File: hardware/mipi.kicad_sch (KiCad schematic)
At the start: 52 parts, among them U4 CCGM1A1, Y1 FNETHE025

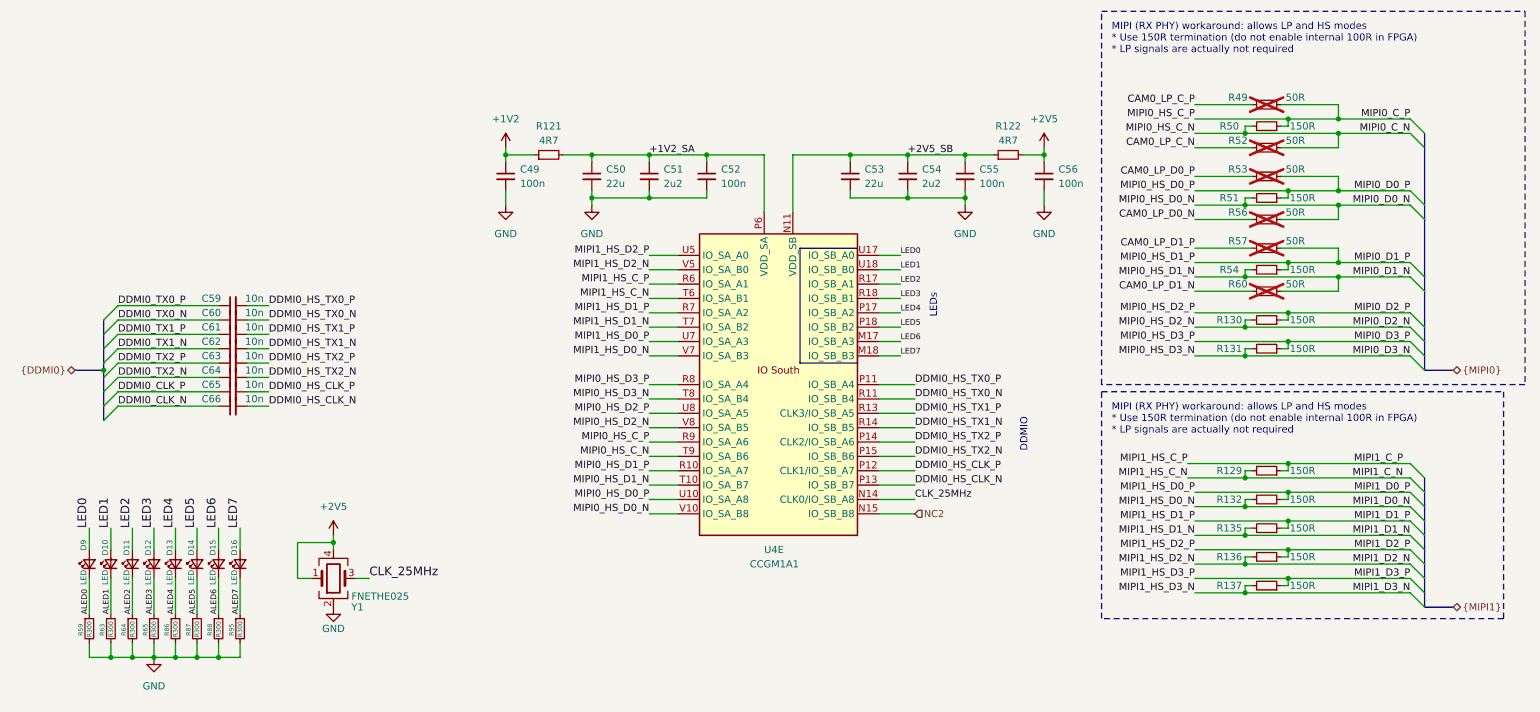
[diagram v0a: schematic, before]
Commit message: Clearing ERC errors/warnings
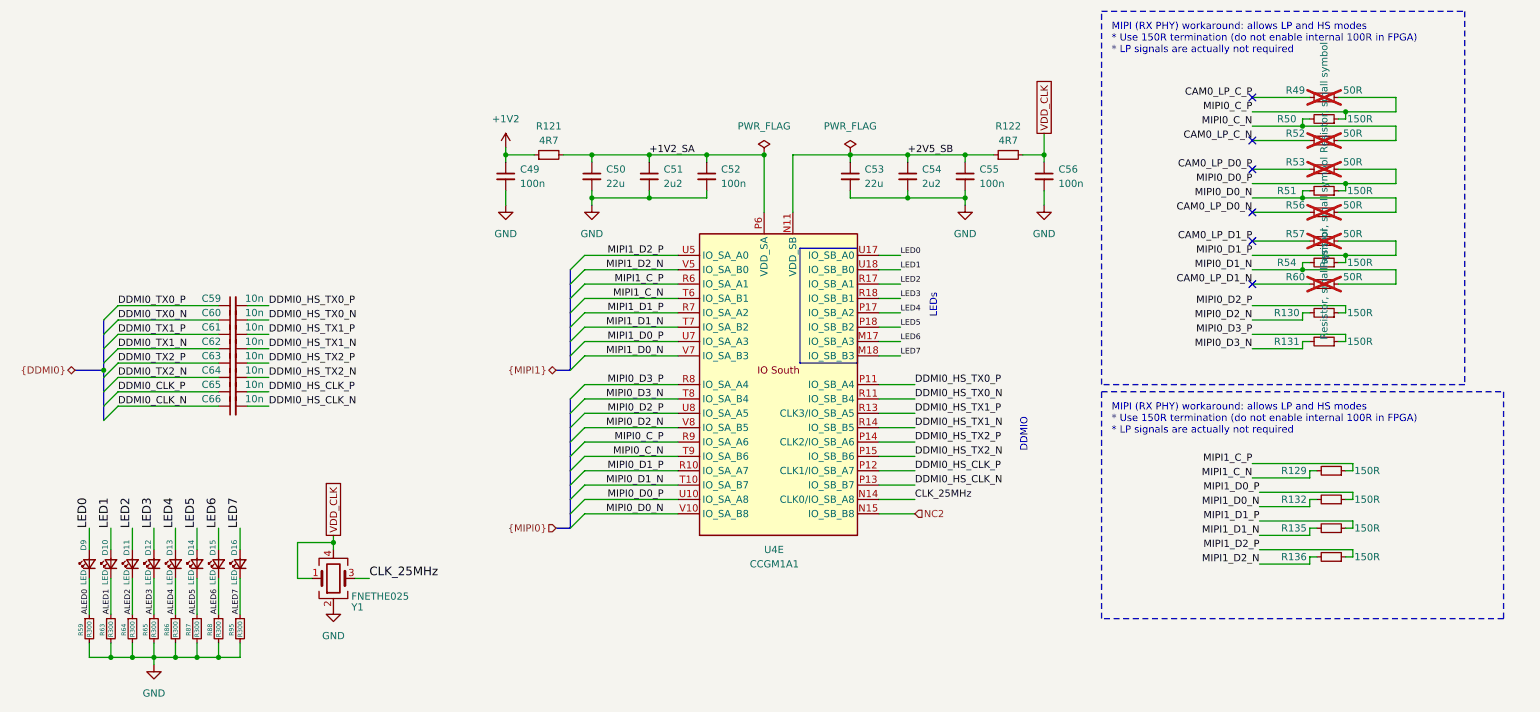
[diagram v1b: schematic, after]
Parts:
- removed R137: 150R, Resistor_SMD:R_0402_1005Metric, symbol Device:R_Small
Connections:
- net +2V5 renamed VDD_CLK
- no-connect marks 0 -> 6
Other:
- moved on the sheet: R129, R130, R131, R132, R135, R136, R49, R50, R51, R52, R53, R54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

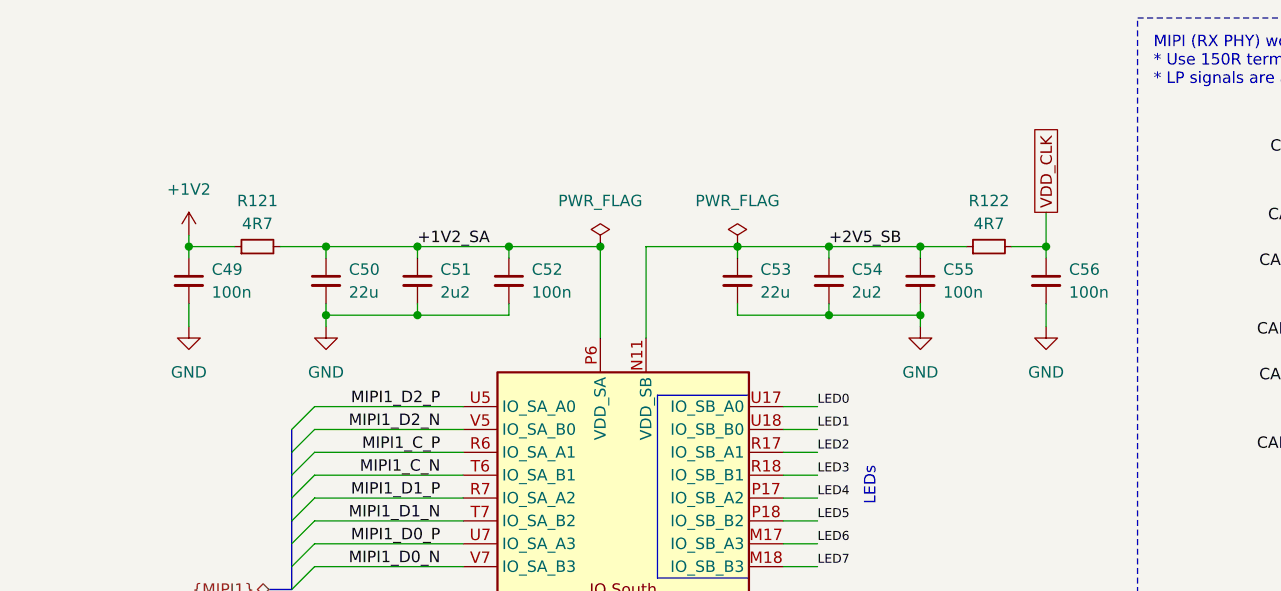
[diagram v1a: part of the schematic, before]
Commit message: Clearing all ERC, rounting diff
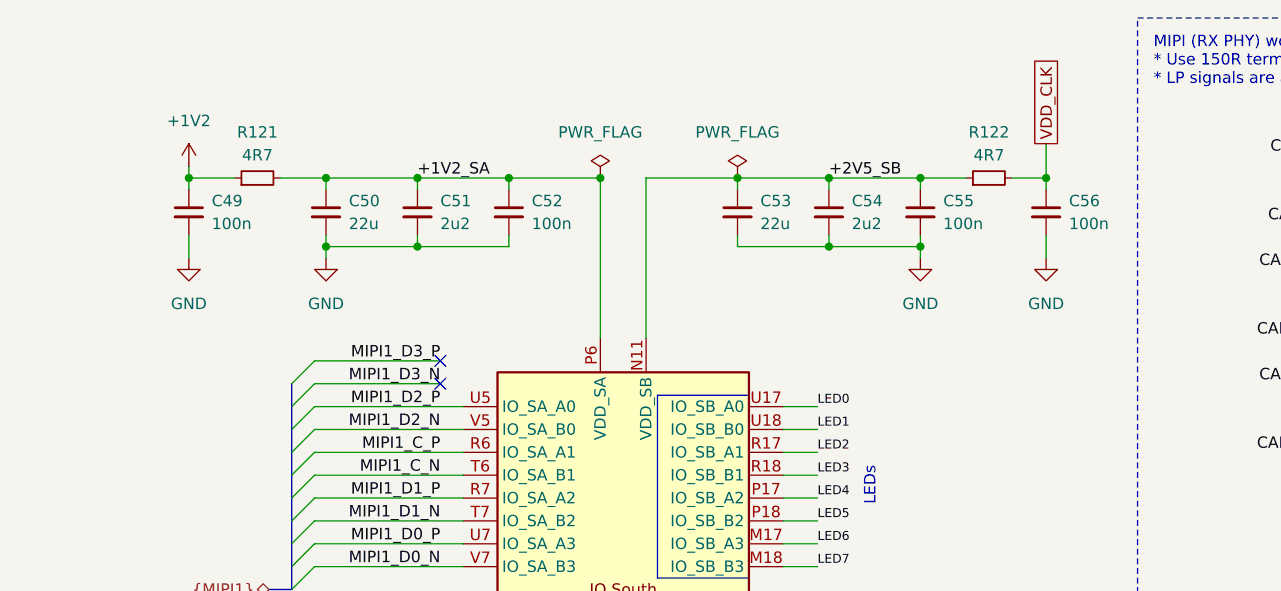
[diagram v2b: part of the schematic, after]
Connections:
- no-connect marks 6 -> 8
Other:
- moved on the sheet: C49, C50, C51, C52, C53, C54, C55, C56, R121, R122

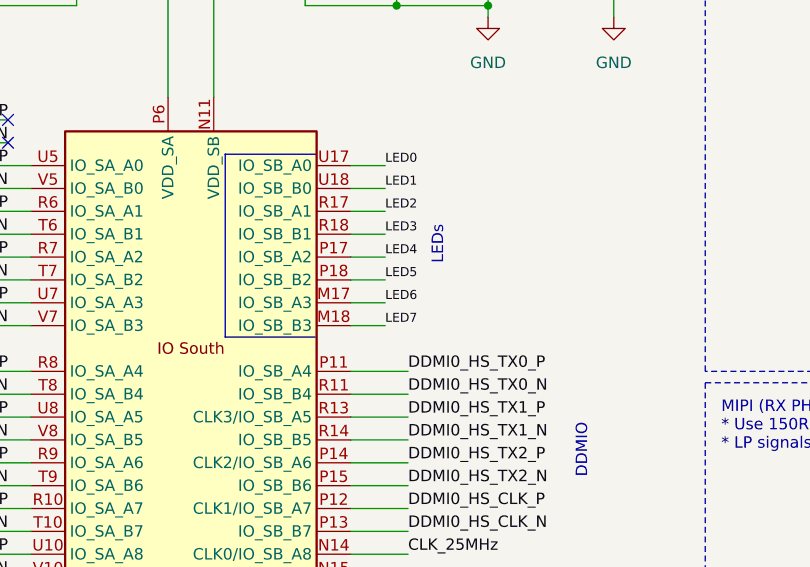
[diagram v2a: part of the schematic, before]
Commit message: Routing BTNs, LEDs, CLK
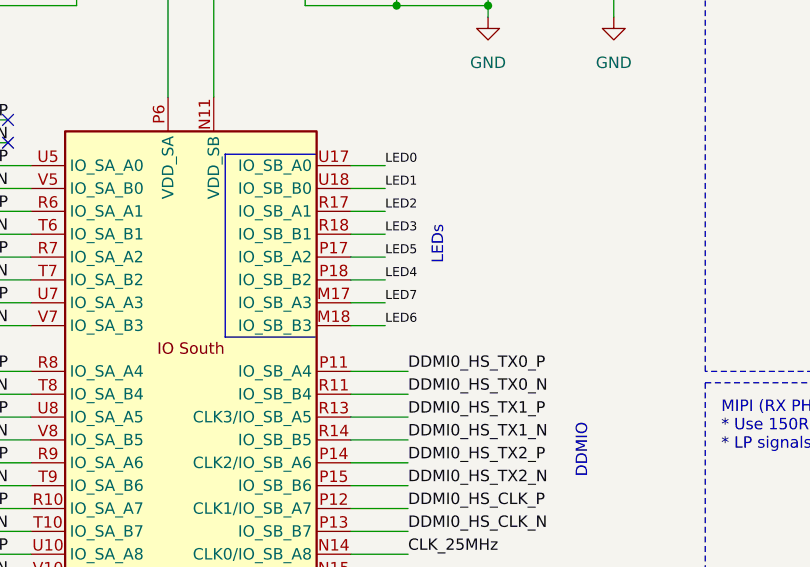
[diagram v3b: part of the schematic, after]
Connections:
- net LED4: now also U4.P18 (IO_SB_B2); no longer U4.P17 (IO_SB_A2)
- net LED5: now also U4.P17 (IO_SB_A2); no longer U4.P18 (IO_SB_B2)
- net LED6: now also U4.M18 (IO_SB_B3); no longer U4.M17 (IO_SB_A3)
- net LED7: now also U4.M17 (IO_SB_A3); no longer U4.M18 (IO_SB_B3)
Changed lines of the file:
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@@
 	)
 	(label "LED6"
-		(at 173.99 71.12 0)
+		(at 173.99 73.66 0)
 		(effects
 			(font
@@
 	)
 	(label "LED7"
-		(at 173.99 73.66 0)
+		(at 173.99 71.12 0)
 		(effects
 			(font
@@
 	)
 	(label "LED4"
-		(at 173.99 66.04 0)
+		(at 173.99 68.58 0)
 		(effects
 			(font
@@
 	)
 	(label "LED5"
-		(at 173.99 68.58 0)
-		(effects
-			(font
+		(at 173.99 66.04 0)
+		(effects
+			(font

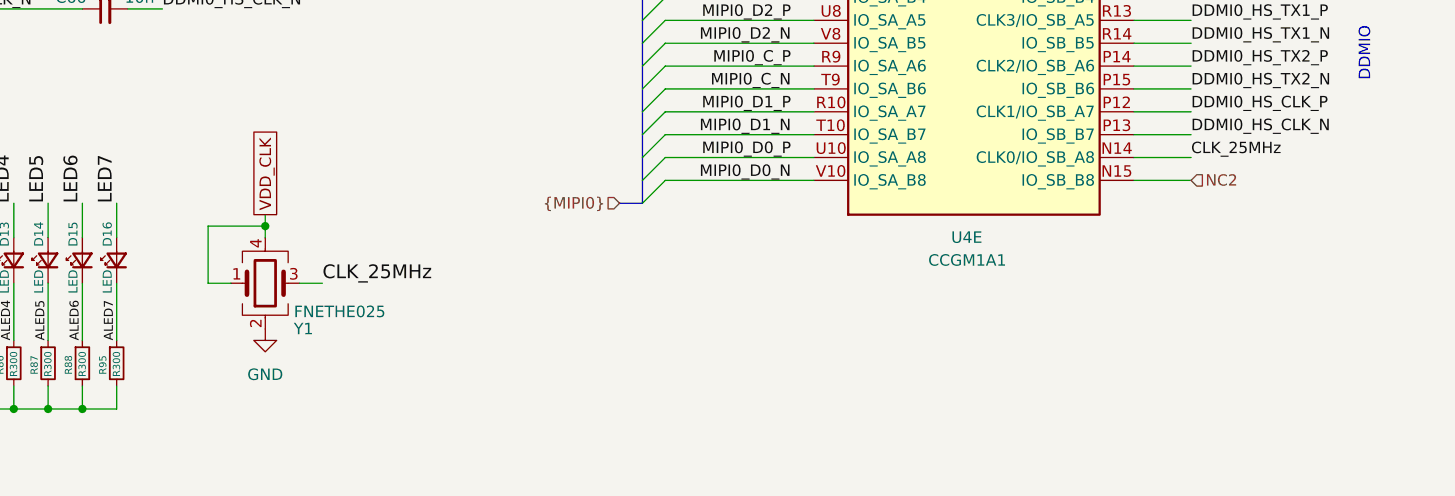
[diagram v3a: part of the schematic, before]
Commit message: Connecting PWR and FAN_PWM to NC pins, using NC3 for Ethernet clock
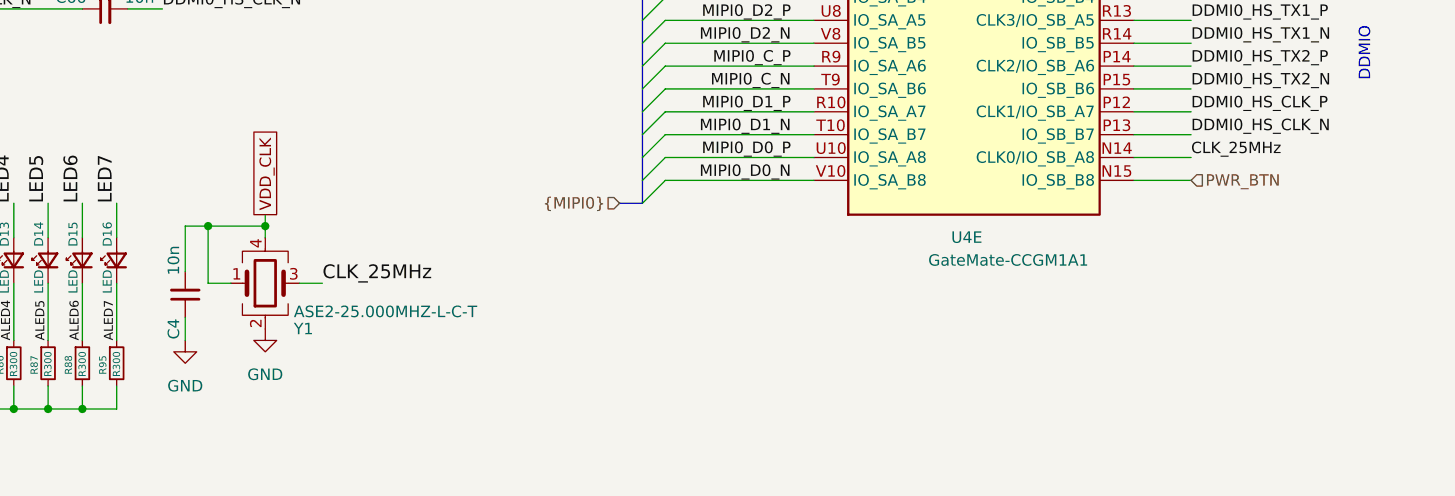
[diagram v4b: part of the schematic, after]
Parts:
- added C4: 10n, Capacitor_SMD:C_0402_1005Metric, symbol Device:C_Small
- U4: value CCGM1A1 -> GateMate-CCGM1A1
- Y1: value FNETHE025 -> ASE2-25.000MHZ-L-C-T; Digikey FNETHE025CT-ND -> (none); Koncar FQ001 -> (none); LCSC C390569 -> (none); MNF1_URL www.diodes.com -> https://eu.mouser.com/ProductDetail/ABRACON/ASE2-25.000MHZ-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; MNF3_URL https://datasheet.lcsc.com/szlcsc/1912111437_Shenzhen-SCTF-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 -> (none); MPN FNETHE025 -> ASE2-25.000MHZ-L-C-T; MPN2 SiT8008BC-81-33E-25.000000X -> (none); MPN3 S7D25.000000D20F30T -> (none); Mouse_r2 788-8008BC8133E25X -> (none); Mouser 729-FNETHE025 -> (none); Newark 80AC8624 -> (none); Side T -> (none); price100_Digikey 0.7942$ -> (none)
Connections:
- net GND: now also C4.1
- net VDD_CLK: now also C4.2
- net NC2 renamed PWR_BTN
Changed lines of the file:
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@@
 	)
 	(junction
+		(at 67.31 106.68)
+		(diameter 0)
+		(color 0 0 0 0)
+	)
+	(junction
 		(at 175.26 38.1)
 		(diameter 0)
@@
 	(wire
 		(pts
+			(xy 64.77 119.38) (xy 64.77 116.84)
+		)
+		(stroke
+			(width 0)
+			(type default)
+		)
+	)
+	(wire
+		(pts
 			(xy 251.46 53.34) (xy 261.62 53.34)
 		)
@@
 	(wire
 		(pts
+			(xy 64.77 111.76) (xy 64.77 106.68)
+		)
+		(stroke
+			(width 0)
+			(type default)
+		)
+	)
+	(wire
+		(pts
 			(xy 245.11 71.12) (xy 245.11 72.39)
 		)
@@
 	(wire
 		(pts
+			(xy 64.77 106.68) (xy 67.31 106.68)
+		)
+		(stroke
+			(width 0)
+			(type default)
+		)
+	)
+	(wire
+		(pts
 			(xy 236.22 53.34) (xy 246.38 53.34)
 		)
@@
 		)
 	)
-	(hierarchical_label "NC2"
+	(hierarchical_label "PWR_BTN"
 		(shape input)
 		(at 176.53 101.6 0)
@@
 			)
 		)
-		(property "Value" "FNETHE025"
+		(property "Value" "ASE2-25.000MHZ-L-C-T"
 			(at 76.835 116.205 0)
 			(effects
@@
 			)
 		)
-		(property "Datasheet" "https://www.diodes.com/assets/Datasheets/FNETHE025.pdf"
+		(property "Datasheet" "https://eu.mouser.com/datasheet/2/3/ASE2series-3624434.pdf"
 			(at 73.66 113.03 0)
 			(effects
@@
 			)
 		)
-		(property "MNF1_URL" "www.diodes.com"
+		(property "MNF1_URL" "https://eu.mouser.com/ProductDetail/ABRACON/ASE2-25.000MHZ-L-C-T?qs=s46Hw6dZPL6z06Y74PH7Lg%3D%3D"
 			(at 73.66 113.03 0)
 			(effects
@@
 			)
 		)
-		(property "MPN" "FNETHE025"
+		(property "MPN" "ASE2-25.000MHZ-L-C-T"
 			(at 73.66 113.03 0)
 			(effects
@@
 			)
 		)
-		(property "MPN2" "SiT8008BC-81-33E-25.000000X"
+		(property "MPN2" ""
 			(at 73.66 113.03 0)
 			(effects
@@
 			)
 		)
-		(property "MNF3_URL" "https://datasheet.lcsc.com/szlcsc/1912111437_Shenzhen-SCTF-Elec-S7D25-000000D20F30T_C387026.pdf"
+		(property "MNF3_URL" ""
 			(at 73.66 113.03 0)
 			(effects
@@
 			)
 		)
-		(property "MPN3" "S7D25.000000D20F30T"
+		(property "MPN3" ""
 			(at 73.66 113.03 0)
 			(effects
@@
 			)
 		)
-		(property "Mouser" "729-FNETHE025"
+		(property "Mouser" ""
 			(at 73.66 113.03 0)
 			(effects
@@
 			)
 		)
-		(property "Mouse_r2" "788-8008BC8133E25X "
+		(property "Mouse_r2" ""
 			(at 73.66 113.03 0)
 			(effects
@@
 			)
 		)
-		(property "Digikey" "FNETHE025CT-ND"
+		(property "Digikey" ""
 			(at 73.66 113.03 0)
 			(effects
@@
 			)
 		)
-		(property "Newark" "80AC8624"
+		(property "Newark" ""
 			(at 73.66 113.03 0)
 			(effects
@@
 			)
 		)
-		(property "LCSC" "C390569"
+		(property "LCSC" ""
 			(at 73.66 113.03 0)
 			(effects
@@
 			)
 		)
-		(property "price100_Digikey" "0.7942$"
+		(property "price100_Digikey" ""
 			(at 73.66 113.03 0)
 			(effects
@@
 			)
 		)
-		(property "Koncar" "FQ001"
+		(property "Koncar" ""
 			(at 73.66 113.03 0)
 			(effects
@@
 			)
 		)
-		(property "Side" "T"
+		(property "Side" ""
 			(at 73.66 113.03 0)
 			(effects
@@
 	)
 	(symbol
+		(lib_id "Device:C_Small")
+		(at 64.77 114.3 180)
+		(unit 1)
+		(exclude_from_sim no)
+		(in_bom yes)
+		(on_board yes)
+		(dnp no)
+		(property "Reference" "C4"
+			(at 63.5 118.11 90)
+			(effects
+				(font
+					(size 1.27 1.27)
+				)
+			)
+		)
+		(property "Value" "10n"
+			(at 63.5 110.49 90)
+			(effects
+				(font
+					(size 1.27 1.27)
+				)
+			)
+		)
+		(property "Footprint" "Capacitor_SMD:C_0402_1005Metric"
+			(at 64.77 114.3 0)
+			(effects
+				(font
+					(size 1.27 1.27)
+				)
+				(hide yes)
+			)
+		)
+		(property "Datasheet" "~"
+			(at 64.77 114.3 0)
+			(effects
+				(font
+					(size 1.27 1.27)
+				)
+				(hide yes)
+			)
+		)
+		(property "Description" ""
+			(at 64.77 114.3 0)
+			(effects
+				(font
+					(size 1.27 1.27)
+				)
+			)
+		)
+		(pin "1"
+		)
+		(pin "2"
+		)
+		(instances
+			(project "ulx5m-gs"
+				(path "/9e5cbfd6-8186-4817-919e-acd256336bc8/b5a4e16b-0077-47a1-907a-7465e5b4a9ce"
+					(reference "C4")
+					(unit 1)
+				)
+			)
+		)
+	)
+	(symbol
 		(lib_id "power:GND")
 		(at 119.38 39.37 0)
@@
 			)
 		)
-		(property "Value" "CCGM1A1"
+		(property "Value" "GateMate-CCGM1A1"
 			(at 147.32 110.49 0)
 			(effects
@@
 					(unit 1)
 				)
+			)
+		)
+	)
+	(symbol
+		(lib_id "power:GND")
+		(at 64.77 119.38 0)
+		(unit 1)
+		(exclude_from_sim no)
+		(in_bom yes)
+		(on_board yes)
+		(dnp no)
+		(fields_autoplaced yes)
+		(property "Reference" "#PWR059"
+			(at 64.77 125.73 0)
+			(effects
+				(font
+					(size 1.27 1.27)
+				)
+				(hide yes)
+			)
+		)
+		(property "Value" "GND"
+			(at 64.77 124.46 0)
+			(effects
+				(font
+					(size 1.27 1.27)
+				)
+			)
+		)
+		(property "Footprint" ""
+			(at 64.77 119.38 0)
+			(effects
+				(font
+					(size 1.27 1.27)
+				)
+				(hide yes)
+			)
+		)
+		(property "Datasheet" ""
+			(at 64.77 119.38 0)
+			(effects
+				(font
+					(size 1.27 1.27)
+				)
+				(hide yes)
+			)
+		)
+		(property "Description" "Power symbol creates a global label with name \"GND\" , ground"
+			(at 64.77 119.38 0)
+			(effects
+				(font
+					(size 1.27 1.27)
+				)
+				(hide yes)
+			)
+		)
+		(pin "1"
+		)
+		(instances
+			(project "ulx5m-gs"
+				(path "/9e5cbfd6-8186-4817-919e-acd256336bc8/b5a4e16b-0077-47a1-907a-7465e5b4a9ce"
+					(reference "#PWR059")
+					(unit 1)
+				)
